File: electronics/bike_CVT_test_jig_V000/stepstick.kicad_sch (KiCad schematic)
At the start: 0 parts

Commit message: schematic entry work in progress
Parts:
- added C2, C4: 1u, SquantorRcl:C_0603, symbol Device:C
- added C3, C5: 100u, symbol Device:C_Polarized
- added R2: 10K, SquantorRcl:R_0603_hand, symbol Device:R
- added U1: stepstick_TMC, SquantorModules:stepstick_18p, symbol SquantorModules:stepstick_TMC
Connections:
- new net Dir: U1.8 (Dir)
- new net GND: C2.2, C3.2, C4.2, C5.2, U1.15 (GND), U1.9 (GND)
- new net MOT_1A: U1.12 (1A)
- new net MOT_1B: U1.11 (1B)
- new net MOT_2A: U1.13 (2A)
- new net MOT_2B: U1.14 (2B)
- new net MS1: U1.2 (MS1)
- new net MS2: U1.3 (MS2)
- new net MS3: U1.4 (!PDN/UART)
- new net Reset: U1.5 (!PDN/UART)
- new net Sleep: U1.6 (various)
- new net Step: U1.7 (Step)
- new net VIO: C4.1, C5.1, R2.1, U1.10 (VIO)
- new net VMOT: C2.1, C3.1, U1.16 (VMOT)
- new net /Enable: R2.2, U1.1 (!Enable)

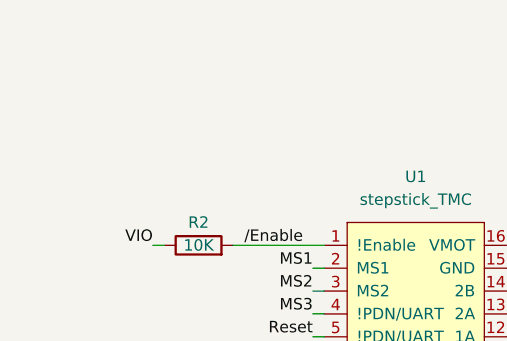
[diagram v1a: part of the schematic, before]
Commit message: added some pins to stepstick, added pi pico library, updated PCB library
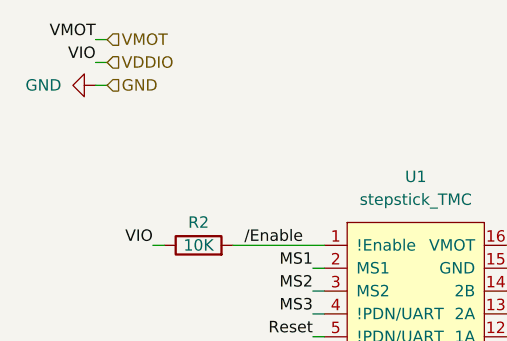
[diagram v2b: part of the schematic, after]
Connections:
- net VIO renamed VDDIO
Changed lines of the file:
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@@
   (junction (at 92.71 67.31) (diameter 0) (color 0 0 0 0)
   )
+  (wire (pts (xy 29.21 20.32) (xy 30.48 20.32))
+    (stroke (width 0) (type default))
+  )
   (wire (pts (xy 104.14 67.31) (xy 104.14 66.04))
     (stroke (width 0) (type default))
@@
     (stroke (width 0) (type default))
   )
+  (wire (pts (xy 29.21 22.86) (xy 30.48 22.86))
+    (stroke (width 0) (type default))
+  )
   (wire (pts (xy 74.93 50.8) (xy 78.74 50.8))
     (stroke (width 0) (type default))
@@
     (stroke (width 0) (type default))
   )
+  (wire (pts (xy 29.21 25.4) (xy 30.48 25.4))
+    (stroke (width 0) (type default))
+  )
   (wire (pts (xy 76.2 58.42) (xy 74.93 58.42))
     (stroke (width 0) (type default))
@@
     (effects (font (size 1.27 1.27)) (justify left bottom))
   )
+  (label "VMOT" (at 29.21 20.32 180) (fields_autoplaced)
+    (effects (font (size 1.27 1.27)) (justify right bottom))
+  )
   (label "MOT_2A" (at 78.74 50.8 0) (fields_autoplaced)
     (effects (font (size 1.27 1.27)) (justify left bottom))
@@
   (label "Reset" (at 53.34 53.34 180) (fields_autoplaced)
     (effects (font (size 1.27 1.27)) (justify right bottom))
+  )
+  (label "VIO" (at 29.21 22.86 180) (fields_autoplaced)
+    (effects (font (size 1.27 1.27)) (justify right bottom))
+  )
+  (hierarchical_label "VMOT" (shape input) (at 30.48 20.32 0) (fields_autoplaced)
+    (effects (font (size 1.27 1.27)) (justify left))
+  )
+  (hierarchical_label "GND" (shape input) (at 30.48 25.4 0) (fields_autoplaced)
+    (effects (font (size 1.27 1.27)) (justify left))
+  )
+  (hierarchical_label "VDDIO" (shape input) (at 30.48 22.86 0) (fields_autoplaced)
+    (effects (font (size 1.27 1.27)) (justify left))
   )
   (symbol (lib_id "Device:C_Polarized") (at 104.14 62.23 0) (unit 1)
@@
         )
       )
+    )
+  )
+  (symbol (lib_id "power:GND") (at 29.21 25.4 270) (unit 1)
+    (in_bom yes) (on_board yes) (dnp no) (fields_autoplaced)
+    (property "Reference" "#PWR07" (at 22.86 25.4 0)
+      (effects (font (size 1.27 1.27)) hide)
+    )
+    (property "Value" "GND" (at 25.4 25.4 90)
+      (effects (font (size 1.27 1.27)) (justify right))
+    )
+    (property "Footprint" "" (at 29.21 25.4 0)
+      (effects (font (size 1.27 1.27)) hide)
+    )
+    (property "Datasheet" "" (at 29.21 25.4 0)
+      (effects (font (size 1.27 1.27)) hide)
+    )
+    (pin "1")
+    (instances
+      (project "bike_CVT_test_jig_V000"
+        (path "/8d9a3ecc-539f-41da-8099-d37cea9c28e7/8841ab6e-b67b-4aac-b2d8-b6b0ccf842b3"
+          (reference "#PWR07") (unit 1)
+        )
+      )
